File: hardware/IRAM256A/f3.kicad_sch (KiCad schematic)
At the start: 34 parts

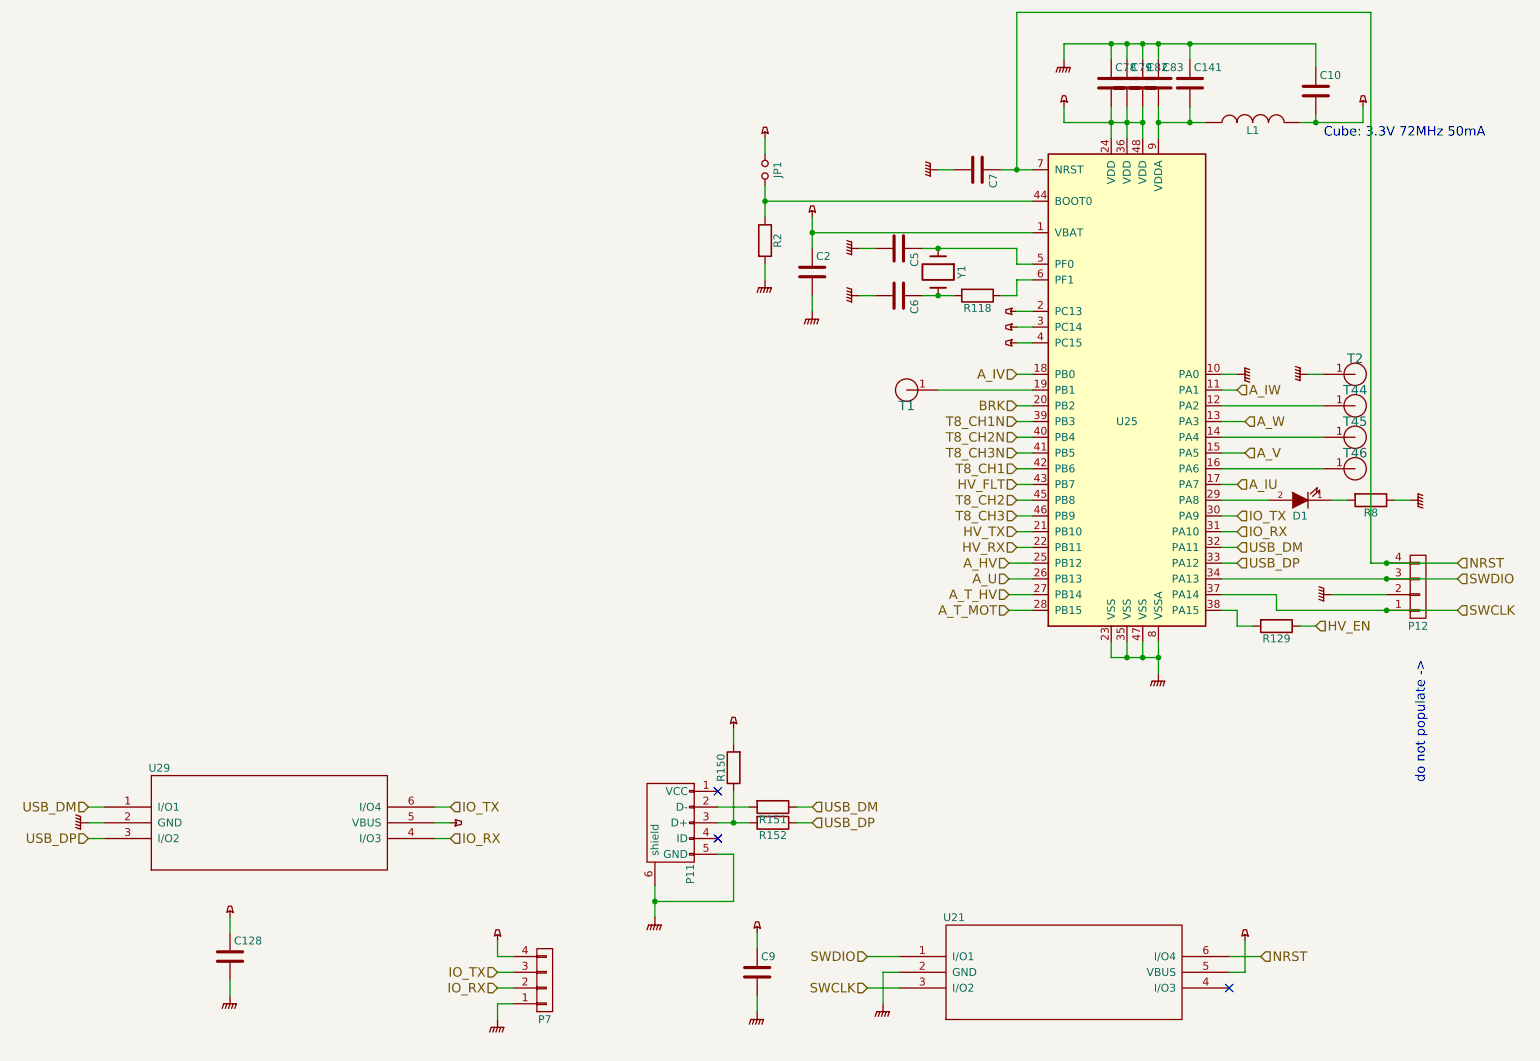
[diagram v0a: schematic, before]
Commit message: Structure change + kicad 3d models updated
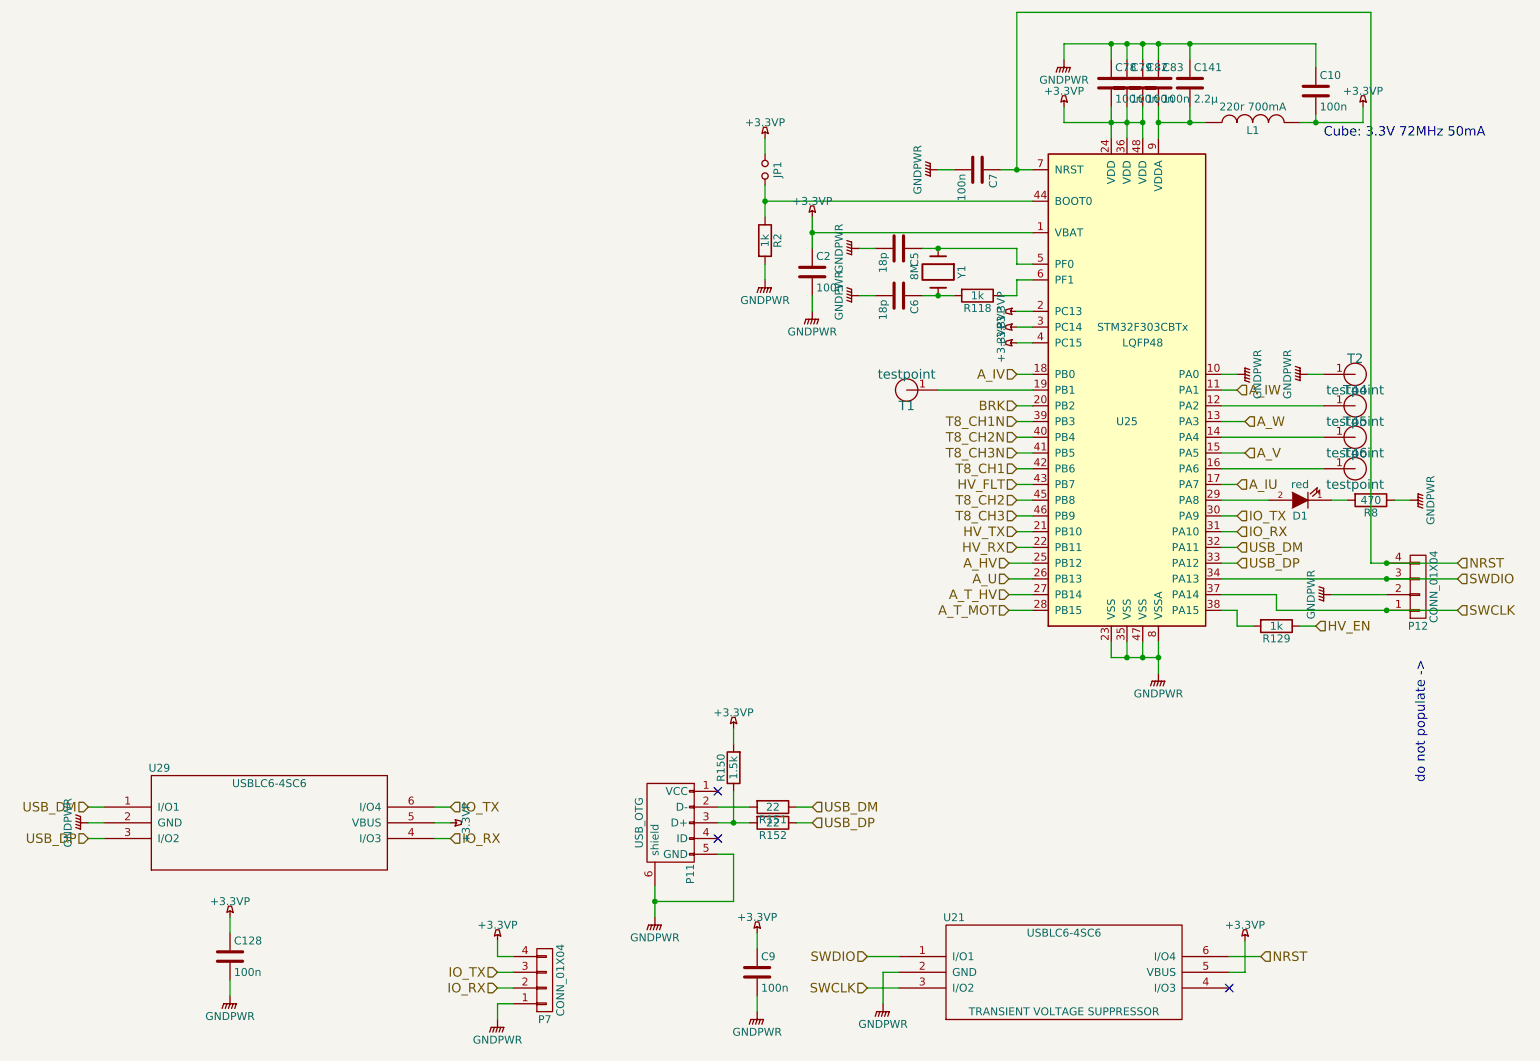
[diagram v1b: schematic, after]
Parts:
- C10, C128, C2, C7, C78, C79, C82, C83, C9: value (none) -> 100n; footprint (none) -> stmbl:C_0603
- C141: value (none) -> 2.2µ; footprint (none) -> stmbl:C_0603
- C5, C6: value (none) -> 18p; footprint (none) -> stmbl:C_0603
- D1: value (none) -> red; footprint (none) -> stmbl:LED-0805-SIDE
- JP1: value (none) -> Jumper_NO_Small; footprint (none) -> stmbl:SOLDER_JUMPER
- L1: value (none) -> 220r 700mA; footprint (none) -> stmbl:R_0603
- P11: value (none) -> USB_OTG; footprint (none) -> stmbl:USB_Micro-B
- P12, P7: value (none) -> CONN_01X04; footprint (none) -> stmbl:Pin_Header_Straight_1x04
- R118, R129, R2: value (none) -> 1k; footprint (none) -> stmbl:R_0603
- R150: value (none) -> 1.5k; footprint (none) -> stmbl:R_0603
- R151, R152: value (none) -> 22; footprint (none) -> stmbl:R_0603
- R8: value (none) -> 470; footprint (none) -> stmbl:R_0603
- T1, T2, T44, T45, T46: value (none) -> testpoint; footprint (none) -> stmbl:Measurement_Point_Round-SMD-Pad_Small
- U21, U29: value (none) -> USBLC6-4SC6; footprint (none) -> stmbl:SOT-23-6
- U25: value (none) -> STM32F303CBTx; footprint (none) -> LQFP48
- Y1: value (none) -> 8M; footprint (none) -> stmbl:Crystal_SMD_0503_4Pads
